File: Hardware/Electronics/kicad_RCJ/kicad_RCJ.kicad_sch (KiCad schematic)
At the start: 76 parts, among them J1 Raspberry_Pi_2_3, J10 Conn_01x04_M1_extra, J11 Conn_01x04_M2_extra, J12 Conn_01x04_M3_extra, J13 Conn_01x04_M4_extra, J14 Conn_01x06_teensy_left_extra, J15 Conn_01x04_teensy_right_extra, J16 Conn_01x07_IO_expander_extra, J17 Conn_02x03_I2C, J18 Conn_02x05_3V3_GND, J19 Conn_02x05_5V_GND, J2 Conn_01x06_IMU_extra, J20 Conn_01x06_BNO085_extra, J21 Conn_01x06_ISM20948_extra, J22 Conn_01x02_LSM5DSOX_LIS3MDL_e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, J23 VBAT_meas_conn, J24 Conn_01x02, J25 Conn_01x02, J26 Conn_01x02, J27 Conn_01x02, J28 Conn_01x02_5V, J29 Conn_01x02_3.3V, J3 Conn_01x02_colsens_interrupt, J30 Conn_01x05_photoresistors, J4 Conn_01x02_5V, J5 Conn_01x02_3V3, J6 Conn_01x02_I2C1, J7 Conn_01x01_LOP, J8 Conn_01x03_IO_expander_interr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, J9 Conn_01x06_LED, M5 Servo1, M6 Servo2, U1 DRV8874, U12 VL53L0/1X, U13 VL53L0/1X, U14 VL53L0/1X, U15 VL53L0/1X, U16 VL53L0/1X, U17 VL53L0/1X, U18 VL53L0/1X, U2 DRV8874, U20 BNO085, U21 ICM20948, U22 LSM6DSOX+LIS3MDL, U23 TCS34725, U24 APDS9960, U25 VL53L0/1X, U3 DRV8874, U4 DRV8874

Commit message: enlarged resistor footprint
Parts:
- R1, R10, R12, R13, R14, R2, R3, R4, R6, R8: footprint Resistor_THT:R_Axial_DIN0207_L6.3mm_D2.5mm_P7.62mm_Horizontal -> Resistor_THT:R_Axial_DIN0207_L6.3mm_D2.5mm_P10.16mm_Horizontal
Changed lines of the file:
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@@
       (effects (font (size 1.27 1.27)) (justify left))
     )
-    (property "Footprint" "Resistor_THT:R_Axial_DIN0207_L6.3mm_D2.5mm_P7.62mm_Horizontal" (at 23.622 219.71 90)
+    (property "Footprint" "Resistor_THT:R_Axial_DIN0207_L6.3mm_D2.5mm_P10.16mm_Horizontal" (at 23.622 219.71 90)
       (effects (font (size 1.27 1.27)) hide)
     )
@@
       (effects (font (size 1.27 1.27)) (justify left))
     )
-    (property "Footprint" "Resistor_THT:R_Axial_DIN0207_L6.3mm_D2.5mm_P7.62mm_Horizontal" (at 23.622 229.87 90)
+    (property "Footprint" "Resistor_THT:R_Axial_DIN0207_L6.3mm_D2.5mm_P10.16mm_Horizontal" (at 23.622 229.87 90)
       (effects (font (size 1.27 1.27)) hide)
     )
@@
       (effects (font (size 1.27 1.27)) (justify left))
     )
-    (property "Footprint" "Resistor_THT:R_Axial_DIN0207_L6.3mm_D2.5mm_P7.62mm_Horizontal" (at 221.742 265.43 90)
+    (property "Footprint" "Resistor_THT:R_Axial_DIN0207_L6.3mm_D2.5mm_P10.16mm_Horizontal" (at 221.742 265.43 90)
       (effects (font (size 1.27 1.27)) hide)
     )
@@
       (effects (font (size 1.27 1.27)) (justify left))
     )
-    (property "Footprint" "Resistor_THT:R_Axial_DIN0207_L6.3mm_D2.5mm_P7.62mm_Horizontal" (at 243.332 135.89 90)
+    (property "Footprint" "Resistor_THT:R_Axial_DIN0207_L6.3mm_D2.5mm_P10.16mm_Horizontal" (at 243.332 135.89 90)
       (effects (font (size 1.27 1.27)) hide)
     )
@@
       (effects (font (size 1.27 1.27)) (justify left))
     )
-    (property "Footprint" "Resistor_THT:R_Axial_DIN0207_L6.3mm_D2.5mm_P7.62mm_Horizontal" (at 216.662 135.89 90)
+    (property "Footprint" "Resistor_THT:R_Axial_DIN0207_L6.3mm_D2.5mm_P10.16mm_Horizontal" (at 216.662 135.89 90)
       (effects (font (size 1.27 1.27)) hide)
     )
@@
       (effects (font (size 1.27 1.27)) (justify left))
     )
-    (property "Footprint" "Resistor_THT:R_Axial_DIN0207_L6.3mm_D2.5mm_P7.62mm_Horizontal" (at 257.302 135.89 90)
+    (property "Footprint" "Resistor_THT:R_Axial_DIN0207_L6.3mm_D2.5mm_P10.16mm_Horizontal" (at 257.302 135.89 90)
       (effects (font (size 1.27 1.27)) hide)
     )
@@
       (effects (font (size 1.27 1.27)) (justify left))
     )
-    (property "Footprint" "Resistor_THT:R_Axial_DIN0207_L6.3mm_D2.5mm_P7.62mm_Horizontal" (at 229.362 265.43 90)
+    (property "Footprint" "Resistor_THT:R_Axial_DIN0207_L6.3mm_D2.5mm_P10.16mm_Horizontal" (at 229.362 265.43 90)
       (effects (font (size 1.27 1.27)) hide)
     )
@@
       (effects (font (size 1.27 1.27)) (justify left))
     )
-    (property "Footprint" "Resistor_THT:R_Axial_DIN0207_L6.3mm_D2.5mm_P7.62mm_Horizontal" (at 248.412 265.43 90)
+    (property "Footprint" "Resistor_THT:R_Axial_DIN0207_L6.3mm_D2.5mm_P10.16mm_Horizontal" (at 248.412 265.43 90)
       (effects (font (size 1.27 1.27)) hide)
     )
@@
       (effects (font (size 1.27 1.27)) (justify left))
     )
-    (property "Footprint" "Resistor_THT:R_Axial_DIN0207_L6.3mm_D2.5mm_P7.62mm_Horizontal" (at 229.362 135.89 90)
+    (property "Footprint" "Resistor_THT:R_Axial_DIN0207_L6.3mm_D2.5mm_P10.16mm_Horizontal" (at 229.362 135.89 90)
       (effects (font (size 1.27 1.27)) hide)
     )
@@
       (effects (font (size 1.27 1.27)) (justify left))
     )
-    (property "Footprint" "Resistor_THT:R_Axial_DIN0207_L6.3mm_D2.5mm_P7.62mm_Horizontal" (at 240.792 265.43 90)
+    (property "Footprint" "Resistor_THT:R_Axial_DIN0207_L6.3mm_D2.5mm_P10.16mm_Horizontal" (at 240.792 265.43 90)
       (effects (font (size 1.27 1.27)) hide)
     )

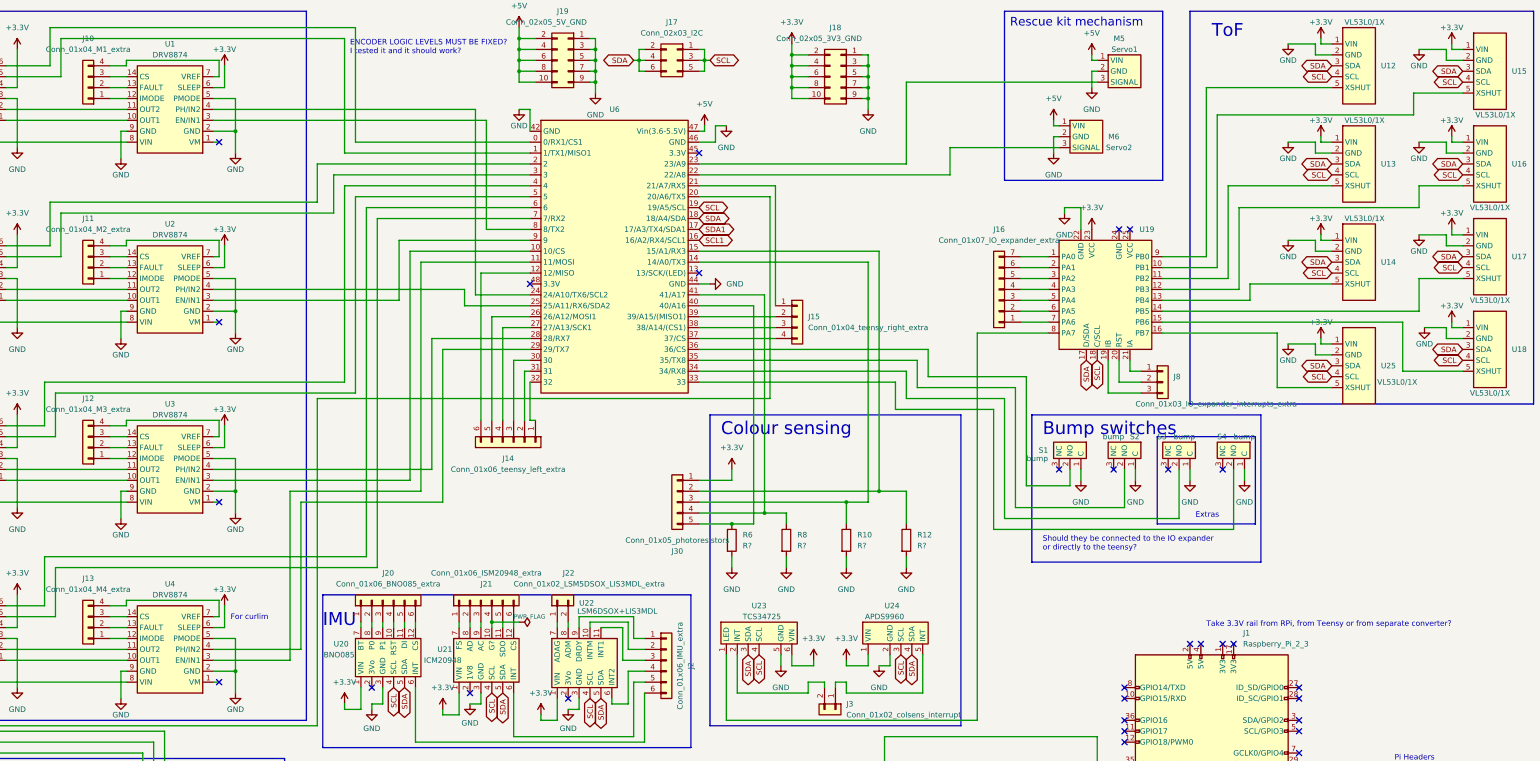
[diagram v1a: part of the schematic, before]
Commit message: continued routing of outer sections and rearranged parts of schematic for better routing
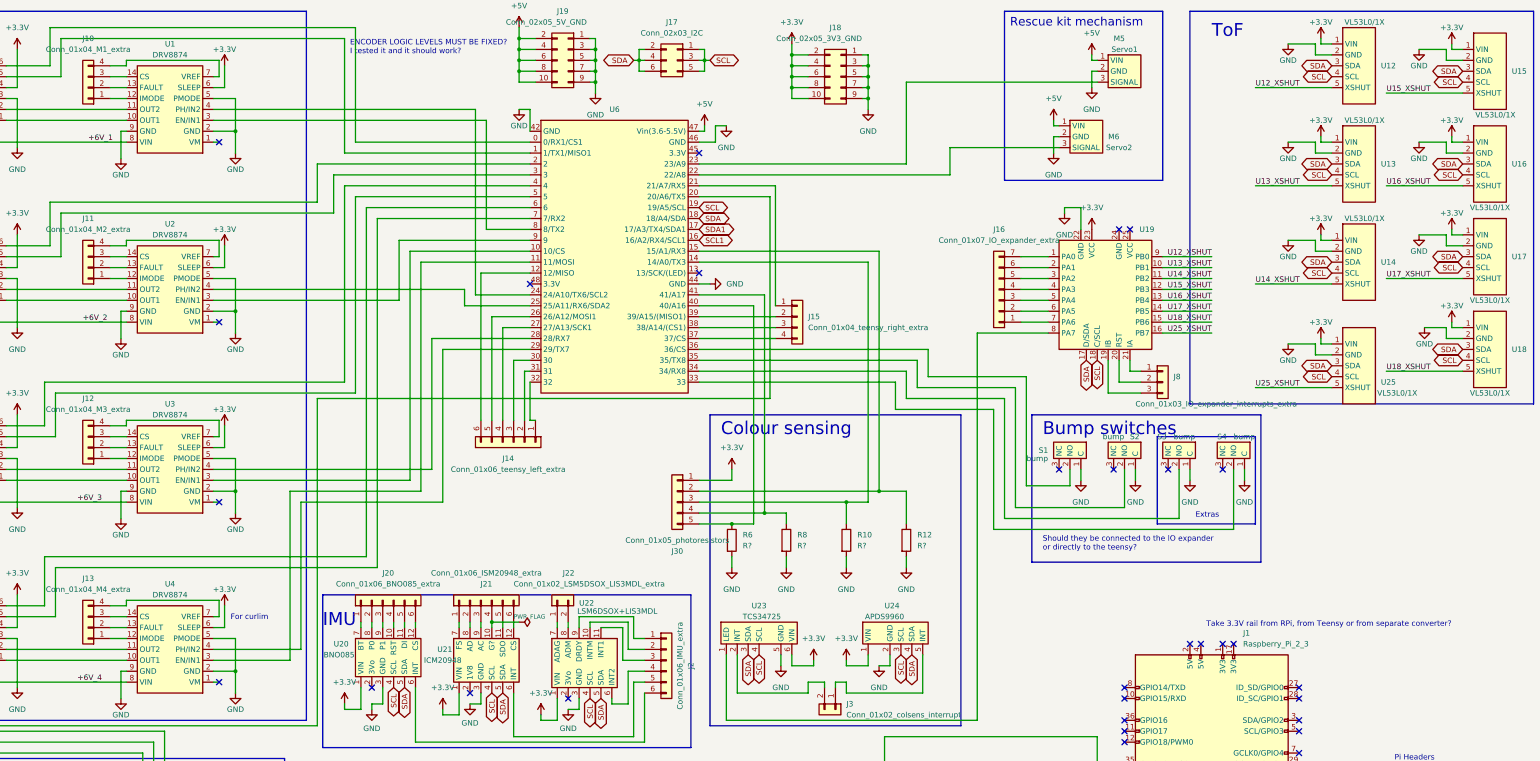
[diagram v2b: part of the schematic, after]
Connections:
- net U13_XSHUT: now reaches U19.10 (PB1)
- net U13_XSHUT: now also U13.5 (XSHUT); no longer U15.5 (XSHUT)
- net U14_XSHUT: now reaches U19.11 (PB2)
- net U14_XSHUT: now also U14.5 (XSHUT); no longer U13.5 (XSHUT)
- net U15_XSHUT: now reaches U19.12 (PB3)
- net U15_XSHUT: now also U15.5 (XSHUT); no longer U16.5 (XSHUT)
- net U16_XSHUT: now reaches U19.13 (PB4)
- net U16_XSHUT: now also U16.5 (XSHUT); no longer U14.5 (XSHUT)
- net U17_XSHUT: now reaches U17.5 (XSHUT), U19.14 (PB5)
- net U18_XSHUT: now reaches U18.5 (XSHUT), U19.15 (PB6)
- net U25_XSHUT: now reaches U19.16 (PB7), U25.5 (XSHUT)
- net U12_XSHUT: now reaches U12.5 (XSHUT), U19.9 (PB0)
- net +6V_1: now reaches J24.2 (Pin_2), U1.8 (VIN)
- net +6V_4: now reaches J27.2 (Pin_2), U4.8 (VIN)
- net +6V_2: now reaches J25.2 (Pin_2), U2.8 (VIN)
- net +6V_3: now reaches J26.2 (Pin_2), U3.8 (VIN)

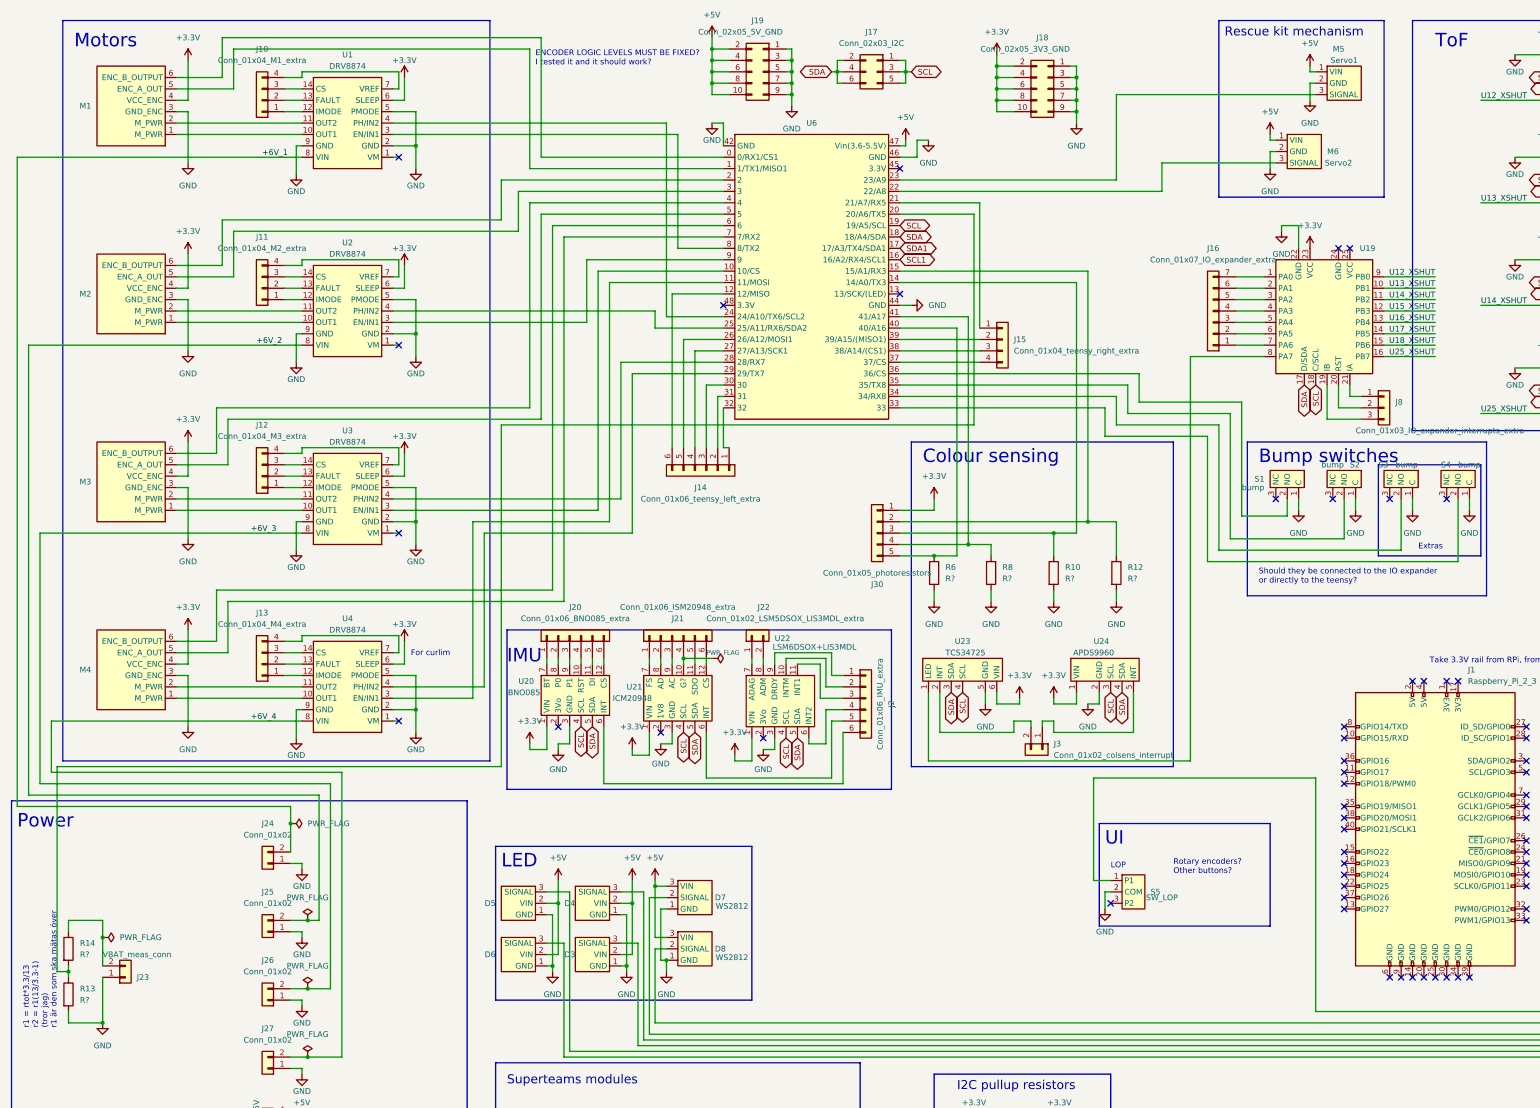
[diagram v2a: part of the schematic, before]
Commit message: finished essential routing (some extras left)
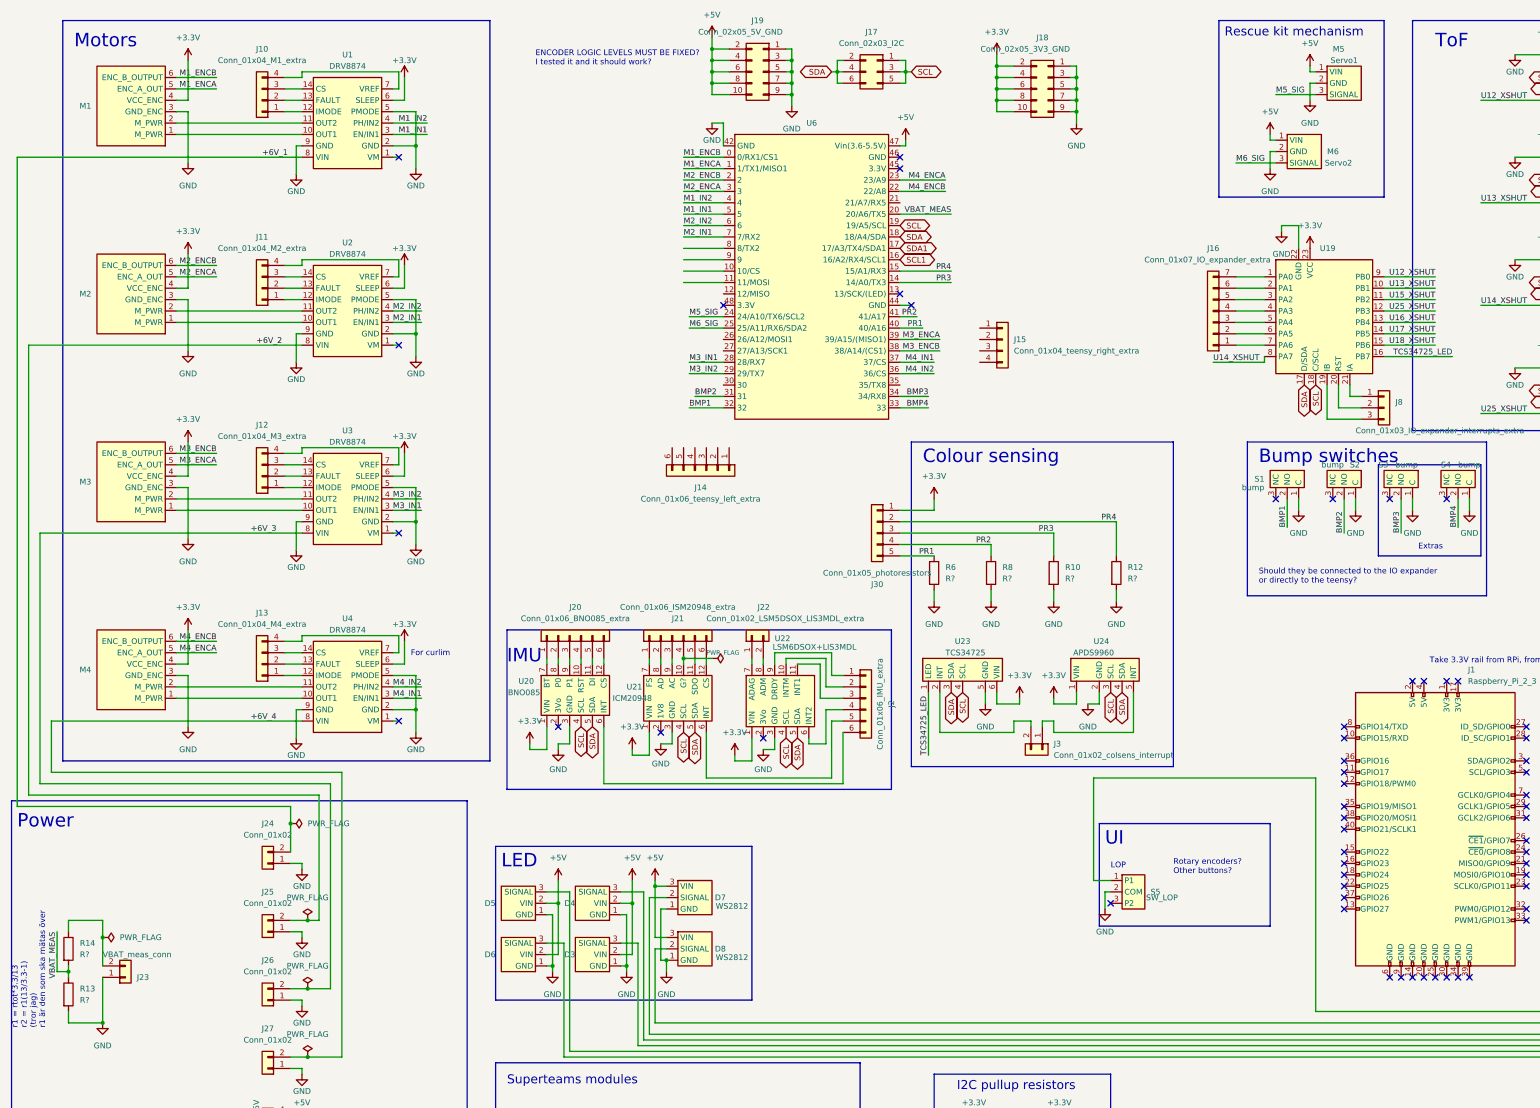
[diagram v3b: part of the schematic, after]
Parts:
- U19: footprint RCJ2024_kicad_footprints:IO_Expander -> RCJ2024_kicad_footprints:IO_Expander_nopower; symbol RCJ_parts:DFRobot_IO_expander -> RCJ_parts:DFRobot_IO_expander_nopower
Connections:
- net GND: no longer U6.44 (GND), U6.46 (GND)
- net U14_XSHUT: now also U19.8 (PA7); no longer U19.11 (PB2)
- net U15_XSHUT: now also U19.11 (PB2); no longer U19.12 (PB3)
- net U25_XSHUT: now also U19.12 (PB3); no longer U19.16 (PB7)
- net TCS34725_LED: now reaches U23.1 (LED)
- net TCS34725_LED: now also U19.16 (PB7); no longer U19.8 (PA7)
- net M2_ENCA: now reaches M2.5 (ENC_A_OUT), U6.3
- net M2_ENCB: now reaches M2.6 (ENC_B_OUTPUT), U6.2
- net BMP3: now reaches S3.2 (NO), U6.34 (34/RX8)
- net VBAT_MEAS: now reaches R13.1, R14.2, U6.20 (20/A6/TX5)
- net BMP1: now reaches S1.2 (NO)
- net BMP1: now also U6.32; no longer U6.36 (36/CS)
- net at U6.8 (8/TX2): no longer U1.3 (EN/IN1)
- net M1_IN2: now reaches U1.4 (PH/IN2)
- net M1_IN2: now also U6.4; no longer U6.24 (24/A10/TX6/SCL2)
- net M4_ENCB: now reaches U6.22 (22/A8)
- net M4_ENCB: now also M4.6 (ENC_B_OUTPUT); no longer M6.3 (SIGNAL)
- net PR3: now reaches J30.3 (Pin_3), R10.1, U6.14 (14/A0/TX3)
- net M1_ENCA: now reaches M1.5 (ENC_A_OUT), U6.1 (1/TX1/MISO1)
- net M1_ENCB: now reaches M1.6 (ENC_B_OUTPUT), U6.0 (0/RX1/CS1)
- net at J14.1 (Pin_1): no longer U6.32
- net at J14.2 (Pin_2): no longer U6.31
- net at J14.3 (Pin_3): no longer U6.30
- net at J14.4 (Pin_4): no longer U6.27 (27/A13/SCK1)
- net at J14.5 (Pin_5): no longer U6.26 (26/A12/MOSI1)
- net at J14.6 (Pin_6): no longer U6.12 (12/MISO)
- net M2_IN1: now reaches U6.7 (7/RX2)
- net M2_IN1: now also U2.3 (EN/IN1); no longer M4.5 (ENC_A_OUT)
- net M2_IN2: now reaches U6.6
- net M2_IN2: now also U2.4 (PH/IN2); no longer M4.6 (ENC_B_OUTPUT)
- net PR1: now reaches J30.5 (Pin_5), R6.1, U6.40 (40/A16)
- net PR4: now reaches J30.2 (Pin_2), R12.1, U6.15 (15/A1/RX3)
- net M4_ENCA: now reaches U6.23 (23/A9)
- net M4_ENCA: now also M4.5 (ENC_A_OUT); no longer M5.3 (SIGNAL)
- net M1_IN1: now reaches U6.5
- net M1_IN1: now also U1.3 (EN/IN1); no longer M3.5 (ENC_A_OUT)
- net M3_ENCB: now reaches M3.6 (ENC_B_OUTPUT)
- net M3_ENCB: now also U6.38 (38/A14/(CS1)); no longer U6.4
- net BMP4: now reaches S4.2 (NO), U6.33
- net at J15.1 (Pin_1): no longer U6.21 (21/A7/RX5)
- net at J15.2 (Pin_2): no longer U6.39 (39/A15/(MISO1))
- net at J15.3 (Pin_3): no longer U6.38 (38/A14/(CS1))
- net at J15.4 (Pin_4): no longer U6.37 (37/CS)
- net at U6.9: no longer U2.3 (EN/IN1)
- net M6_SIG: now reaches U6.25 (25/A11/RX6/SDA2)
- net M6_SIG: now also M6.3 (SIGNAL); no longer U2.4 (PH/IN2)
- net PR2: now reaches J30.4 (Pin_4), R8.1, U6.41 (41/A17)
- net at U6.11 (11/MOSI): no longer U4.3 (EN/IN1)
- net M3_IN2: now reaches U6.29 (29/TX7)
- net M3_IN2: now also U3.4 (PH/IN2); no longer U4.4 (PH/IN2)
- net at U6.10 (10/CS): no longer U3.3 (EN/IN1)
- net M3_IN1: now reaches U6.28 (28/RX7)
- net M3_IN1: now also U3.3 (EN/IN1); no longer U3.4 (PH/IN2)
- net at U6.35 (35/TX8): no longer S2.2 (NO)
- new net BMP2: S2.2 (NO), U6.31
- new net M3_ENCA: M3.5 (ENC_A_OUT), U6.39 (39/A15/(MISO1))
- new net M4_IN1: U4.3 (EN/IN1), U6.37 (37/CS)
- new net M4_IN2: U4.4 (PH/IN2), U6.36 (36/CS)
- new net M5_SIG: M5.3 (SIGNAL), U6.24 (24/A10/TX6/SCL2)

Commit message: PCB finished?
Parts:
- removed J15: Conn_01x04_teensy_right_extra, Connector_PinSocket_2.54mm:PinSocket_1x04_P2.54mm_Vertical, symbol Connector_Generic:Conn_01x04
- added H1, H2, H3, H4, H5, H6, H7: MountingHole, MountingHole:MountingHole_3.2mm_M3, symbol Mechanical:MountingHole
- added J15: Conn_01x03, Connector_PinSocket_2.54mm:PinSocket_1x03_P2.54mm_Vertical, symbol Connector_Generic:Conn_01x03
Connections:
- net at J14.1 (Pin_1): now also U6.12 (12/MISO)
- net at J14.2 (Pin_2): now also U6.11 (11/MOSI)
- net at J14.3 (Pin_3): now also U6.10 (10/CS)
- net at J14.4 (Pin_4): now also U6.9
- net at J14.5 (Pin_5): now also U6.8 (8/TX2)
- net 21_extra: now reaches J14.6 (Pin_6)
- net 21_extra: now also U6.21 (21/A7/RX5)
- net at U6.26 (26/A12/MOSI1): now also J15.3 (Pin_3)
- net at U6.27 (27/A13/SCK1): now also J15.2 (Pin_2)
- net at U6.30: now also J15.1 (Pin_1)
- no-connect marks 57 -> 58
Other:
- moved on the sheet: J14
